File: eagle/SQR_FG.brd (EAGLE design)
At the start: 96.2 x 58.4 mm, 24 parts, among them IC1 MEGA328P, IC2 NJM7032, Q1 16MHz, SW1 EC12E_SW

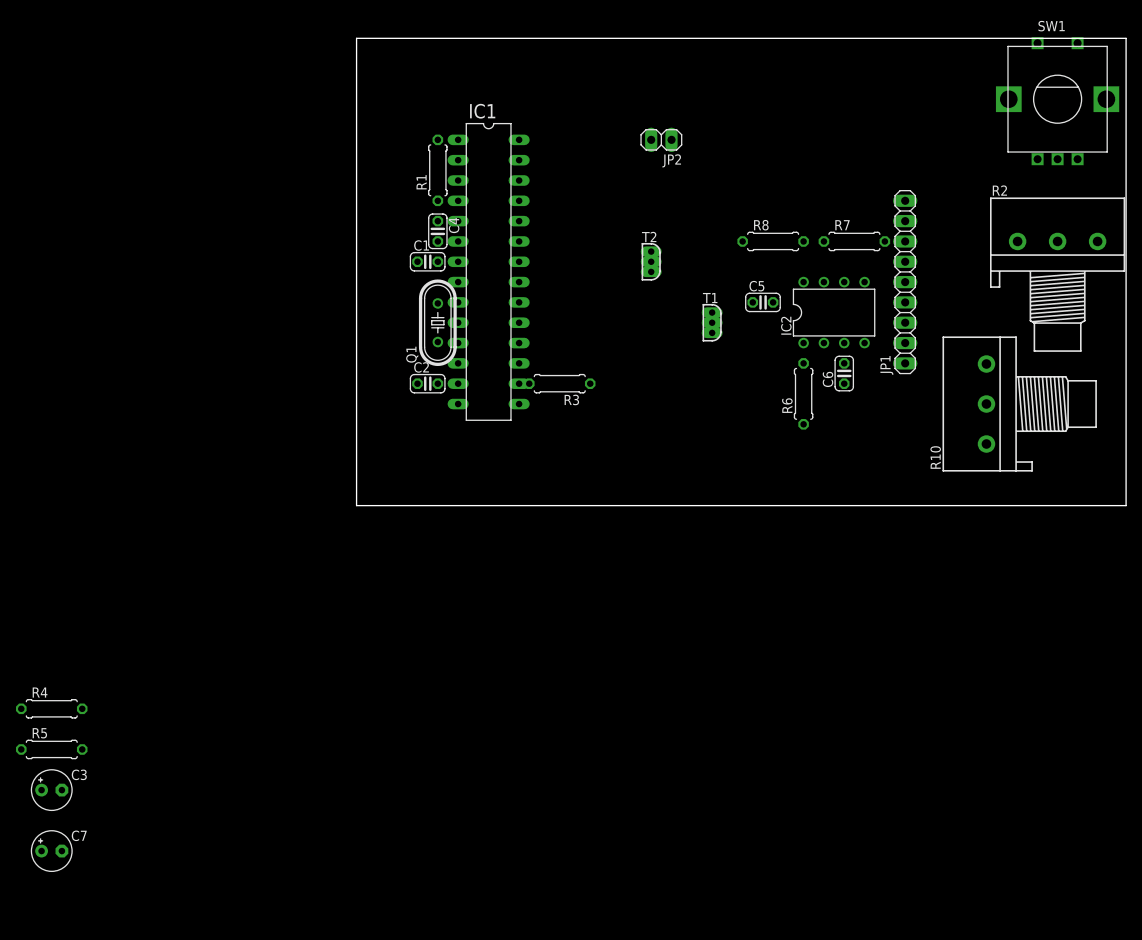
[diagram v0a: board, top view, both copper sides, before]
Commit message: eagle: Add Bypass Connector
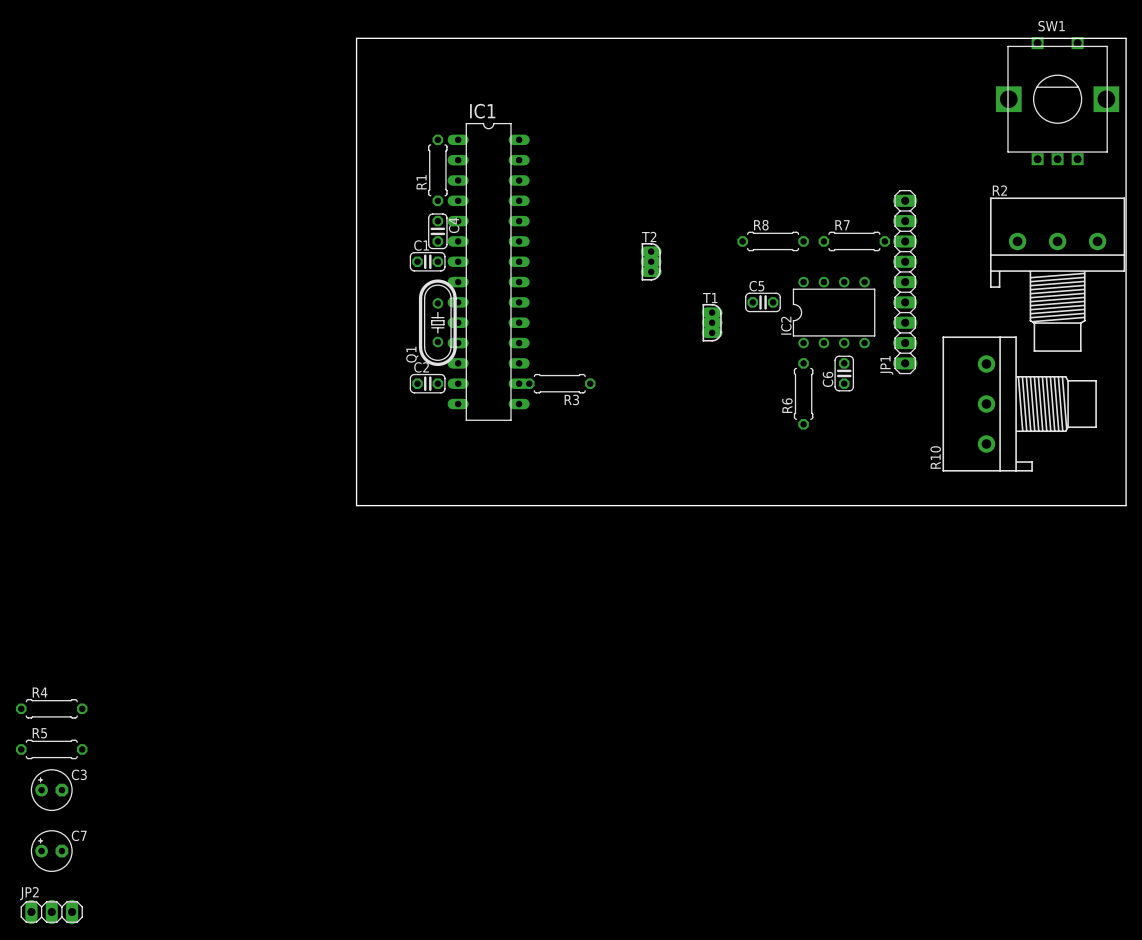
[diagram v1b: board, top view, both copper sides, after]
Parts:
- JP2: value OUT -> OUTPUT; device pinhead:1X02 -> pinhead:1X03
- moved JP2 123.0 mm to (-45.7, -58.4), turned to 0 degrees
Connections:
- net N$11 renamed AMPL
- removed net N$15: C6.2, IC2.3
- removed net N$6: JP2.2, R10.1, T1.1, T2.1
- new net BYPASS: C6.2, IC2.3, JP2.2
- new net GND_OUT: JP2.3, R10.1, T1.1, T2.1
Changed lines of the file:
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@@
 </element>
 <element name="C5" library="rcl" package="C025-024X044" value="0.1uF" x="43.18" y="17.78"/>
-<element name="JP2" library="pinhead" package="1X02" value="OUT" x="30.48" y="38.1" rot="R180"/>
 <element name="R3" library="rcl" package="0207/7" value="33k" x="17.78" y="7.62" rot="R180"/>
 <element name="C6" library="rcl" package="C025-024X044" value="" x="53.34" y="8.89" rot="R90"/>
@@
 <element name="C3" library="rcl" package="E2,5-5" value="100uF" x="-45.72" y="-43.18"/>
 <element name="C7" library="rcl" package="E2,5-5" value="100uF" x="-45.72" y="-50.8"/>
+<element name="JP2" library="pinhead" package="1X03" value="OUTPUT" x="-45.72" y="-58.42"/>
 </elements>
 <signals>
@@
 <wire x1="48.26" y1="2.54" x2="48.26" y2="12.7" width="0" layer="19" extent="1-1"/>
 </signal>
-<signal name="N$11">
+<signal name="AMPL">
 <contactref element="R6" pad="2"/>
 <contactref element="JP2" pad="1"/>
-<wire x1="48.26" y1="10.16" x2="31.75" y2="38.1" width="0" layer="19" extent="1-1"/>
+<wire x1="48.26" y1="10.16" x2="-48.26" y2="-58.42" width="0" layer="19" extent="1-1"/>
 </signal>
 <signal name="N$17">
@@
 <wire x1="55.88" y1="20.32" x2="50.8" y2="25.4" width="0" layer="19" extent="1-1"/>
 </signal>
-<signal name="N$6">
+<signal name="GND_OUT">
 <contactref element="R10" pad="1"/>
 <contactref element="T1" pad="1"/>
 <contactref element="T2" pad="1"/>
-<contactref element="JP2" pad="2"/>
-<wire x1="36.83" y1="13.97" x2="71.12" y2="0.08" width="0" layer="19" extent="1-1"/>
+<contactref element="JP2" pad="3"/>
+<wire x1="36.83" y1="13.97" x2="-43.18" y2="-58.42" width="0" layer="19" extent="1-1"/>
 <wire x1="29.21" y1="21.59" x2="36.83" y2="13.97" width="0" layer="19" extent="1-1"/>
-<wire x1="29.21" y1="38.1" x2="29.21" y2="21.59" width="0" layer="19" extent="1-1"/>
+<wire x1="71.12" y1="0.08" x2="36.83" y2="13.97" width="0" layer="19" extent="1-1"/>
 </signal>
 <signal name="SW_GND">
@@
 <wire x1="36.83" y1="16.51" x2="50.8" y2="20.32" width="0" layer="19" extent="1-1"/>
 </signal>
-<signal name="N$15">
+<signal name="BYPASS">
 <contactref element="C6" pad="2"/>
 <contactref element="IC2" pad="3"/>
-<wire x1="53.34" y1="10.16" x2="53.34" y2="12.7" width="0" layer="19" extent="1-1"/>
+<contactref element="JP2" pad="2"/>
+<wire x1="53.34" y1="10.16" x2="-45.72" y2="-58.42" width="0" layer="19" extent="1-1"/>
+<wire x1="53.34" y1="12.7" x2="53.34" y2="10.16" width="0" layer="19" extent="1-1"/>
 </signal>
 <signal name="AGND">

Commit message: Change eagle SQR_FG.sch R value
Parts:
- R3: value 33k -> 10k
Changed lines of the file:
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@@
 </element>
 <element name="C5" library="rcl" package="C025-024X044" value="0.1uF" x="43.18" y="17.78"/>
-<element name="R3" library="rcl" package="0207/7" value="33k" x="17.78" y="7.62" rot="R180"/>
+<element name="R3" library="rcl" package="0207/7" value="10k" x="17.78" y="7.62" rot="R180"/>
 <element name="C6" library="rcl" package="C025-024X044" value="" x="53.34" y="8.89" rot="R90"/>
 <element name="R4" library="rcl" package="0207/7" value="22k" x="-45.72" y="-33.02"/>

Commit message: SQR_FG.brd SQR_FG board design editing.
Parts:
- removed R10: 10k, pot:3RP/1610N
- removed R2: 10k/B, pot:3RP/1610N
- removed SW1: EC12E_SW, switch-alps:ALPS_EC12E_SW
- added JP3: (no value), pinhead:1X03
- added JP4: Level Vol, pinhead:1X03
- added JP5: (no value), pinhead:1X04
- added JP6: SQR_OUT, pinhead:1X02
- moved C7 133.1 mm to (53.3, 38.1)
- moved C3 122.3 mm to (45.7, 38.1)
- moved JP2 104.7 mm to (35.6, 7.62)
- moved R5 103.3 mm to (29.2, 33.0)
- moved R4 92.5 mm to (19.1, 33.0)
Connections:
- new net N$4: JP4.2, JP6.1
- new net N$5: JP4.1, JP6.2, T1.1, T2.1
- net +5V: now also JP3.1; no longer R2.1
- net GND: now also JP3.3, JP5.4; no longer R2.3, SW1.C, SW1.D
- net GND_OUT: no longer R10.1, T1.1, T2.1
- net N$8: now also JP4.3; no longer R10.3
- net N$9: now also JP3.2; no longer R2.2
- net RE_A: now also JP5.1; no longer SW1.B
- net RE_B: now also JP5.2; no longer SW1.A
- net RE_SW: now also JP5.3; no longer SW1.E
